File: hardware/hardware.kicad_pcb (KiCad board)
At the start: 4 copper layers, 100 parts, among them IC1 TAS5760LDAPR, J2 Conn_01x04, J3 Conn_01x04, J4 USB-C, SW1 SW_Push, SW2 SW_Push, SW3 SW_Push, SW5 SW_Push, U1 TPS563200, U2 ESP32-S3, U3 USBLC6-2SC6, Y1 40MHz, Y2 ABS07-166-32.768KHZ-T

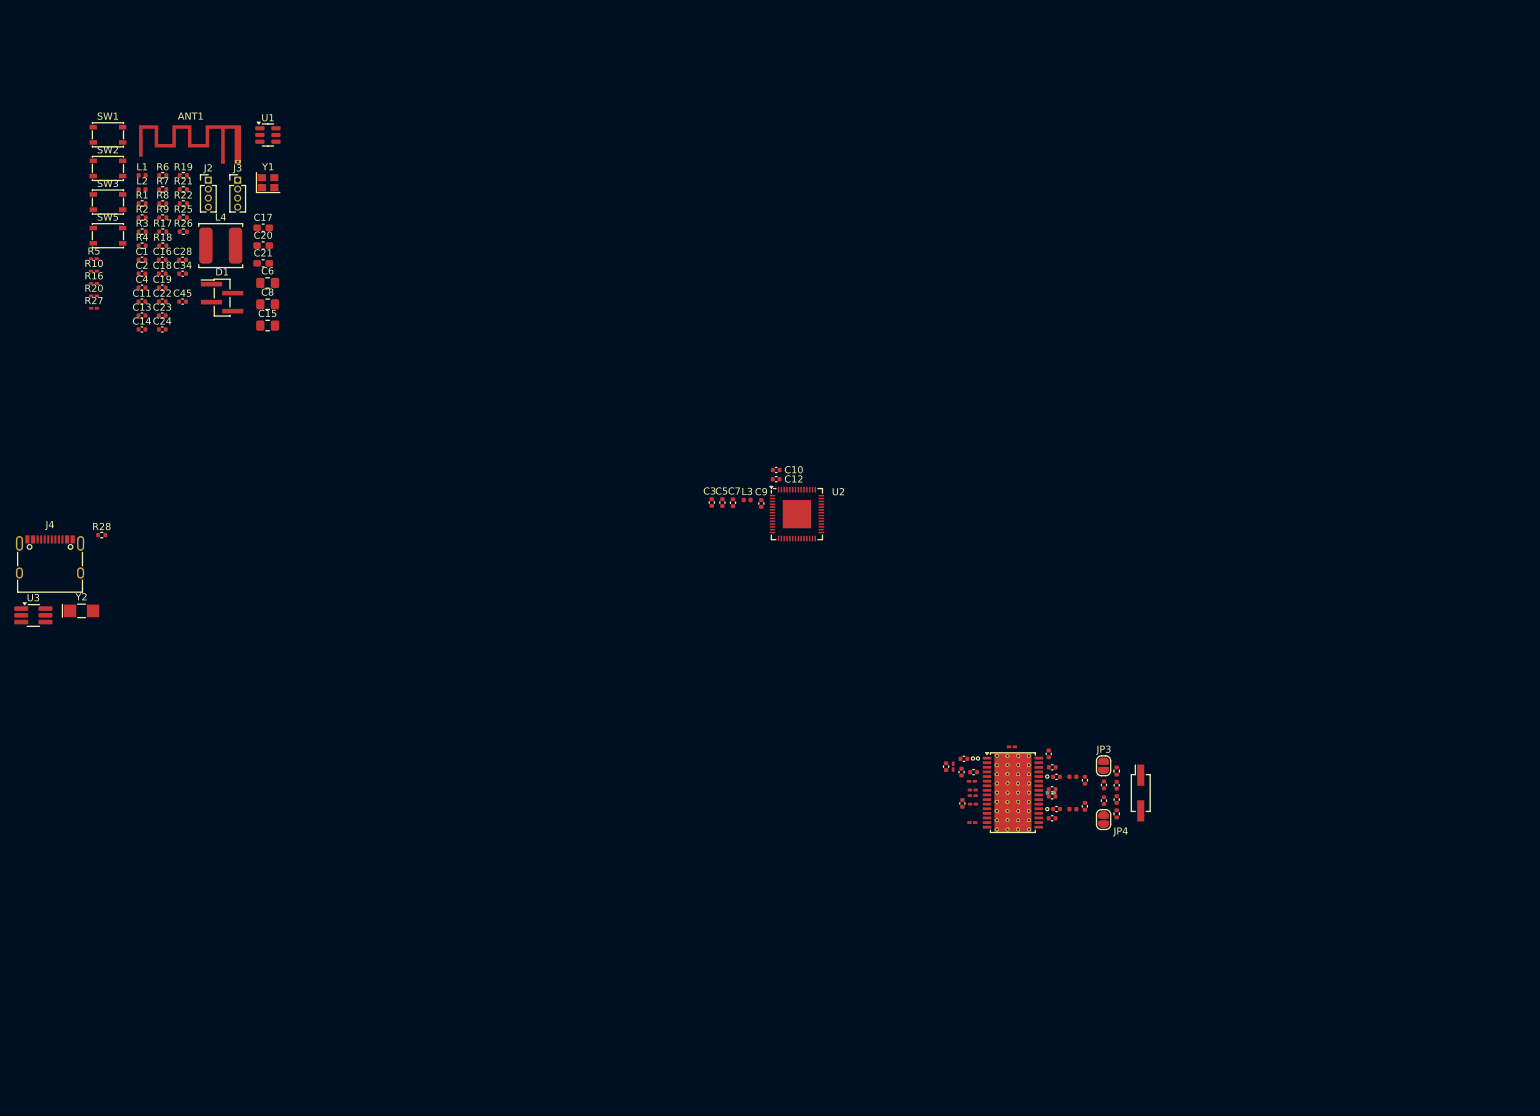
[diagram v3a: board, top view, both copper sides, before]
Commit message: roteamentos do amplificador, perifericos agrupados
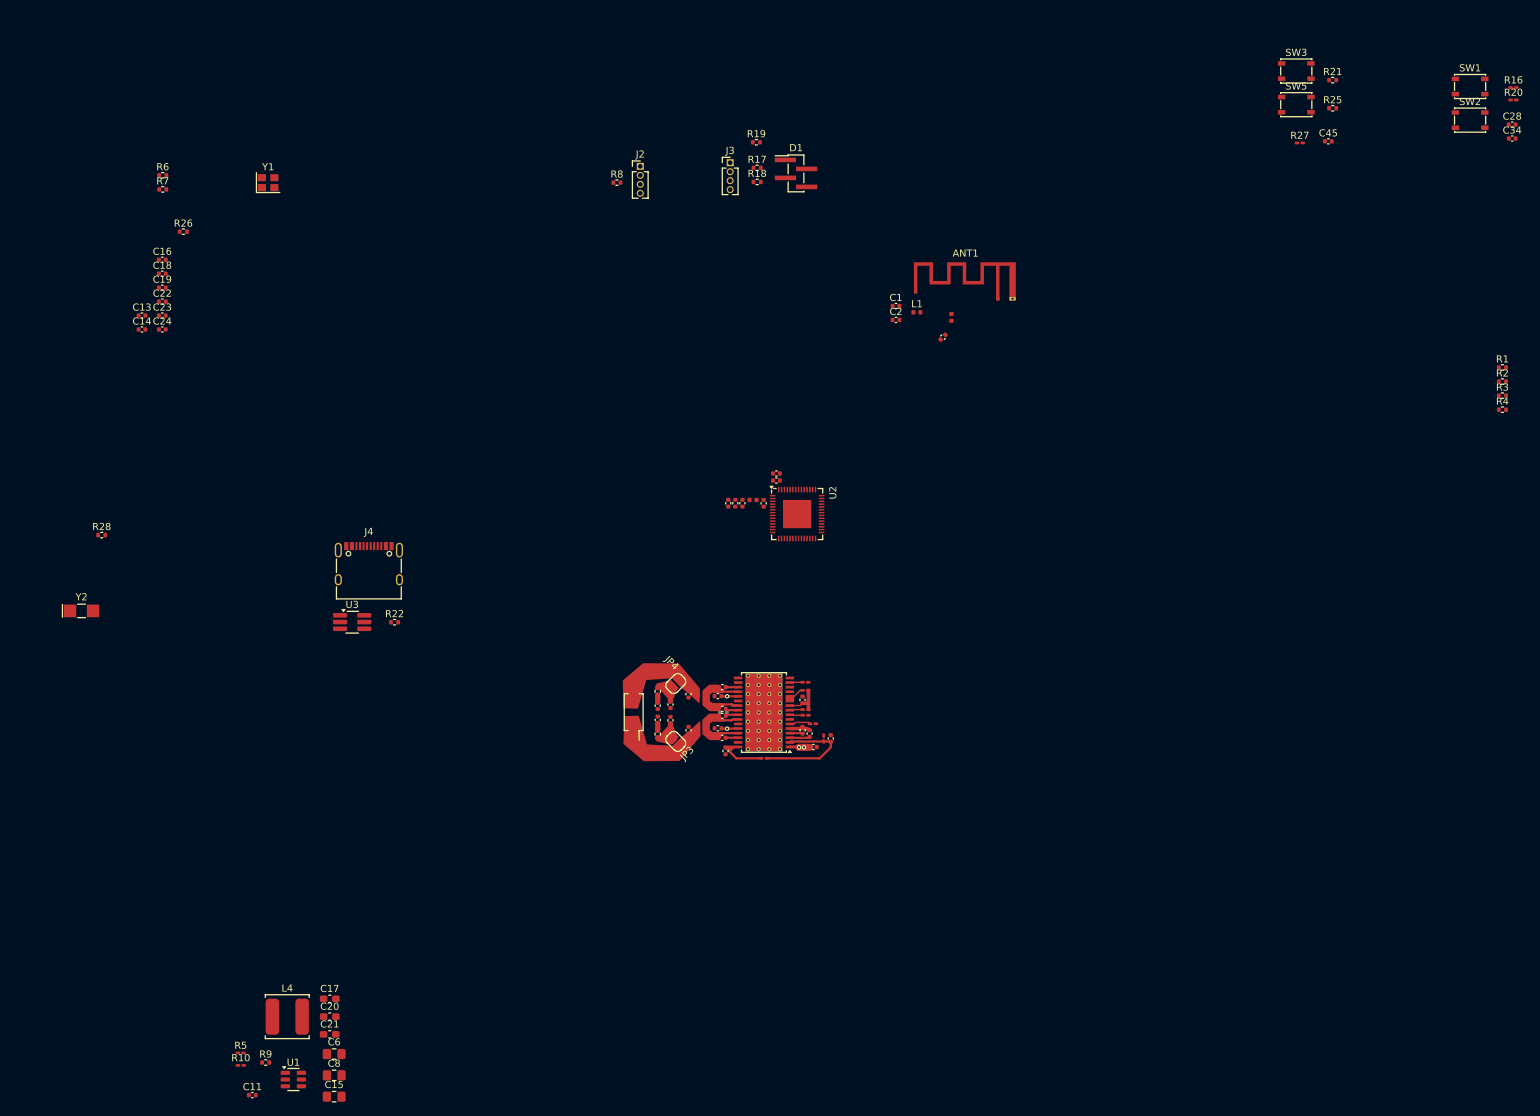
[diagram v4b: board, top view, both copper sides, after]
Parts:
- moved R16 202.4 mm to (240.2, 28.4)
- moved R20 202.4 mm to (240.2, 30.1)
- moved R1 193.5 mm to (238.7, 67.9)
- moved R2 193.5 mm to (238.7, 69.9)
- moved R3 193.5 mm to (238.7, 71.9)
- moved R4 193.5 mm to (238.7, 73.9)
- moved SW1 192.5 mm to (234.1, 28.2)
- moved SW2 192.5 mm to (234.1, 33.0)
- moved C28 188.8 mm to (240.1, 33.6)
- moved C34 188.8 mm to (240.1, 35.6)
- moved R27 171.9 mm to (210.1, 36.2)
- moved SW3 168.9 mm to (209.6, 26.0)
- moved SW5 168.9 mm to (209.6, 30.8)
- moved C45 163.4 mm to (214.1, 36.0)
- moved R21 163.1 mm to (214.7, 27.3)
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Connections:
- U2 pad 10: AUDIO_MUTE -> JTAG
- U2 pad 11: AUDIO_CLK -> AUDIO_EN
- U2 pad 12: I2C_CLK -> AUDIO_FAULT
- U2 pad 13: SDIN -> BOOT
- U2 pad 14: LRCK -> EN
- U2 pad 4: EN -> LRCK
- U2 pad 5: BOOT -> SDIN
- U2 pad 6: AUDIO_FAULT -> I2C_CLK
- U2 pad 7: AUDIO_EN -> AUDIO_CLK
- U2 pad 8: JTAG -> AUDIO_MUTE
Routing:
- net Net-(IC1-SFT_CLIP): track 0.00 -> 16.1 mm
- net Net-(IC1-SPK_OUTB+): track 0.00 -> 15.1 mm
- net Net-(IC1-SPK_OUTA+): track 0.00 -> 13.6 mm
- net Net-(JP4-A): track 0.00 -> 11.8 mm
- net Net-(JP3-B): track 0.00 -> 11.7 mm
- net 8V: track 0.00 -> 9.12 mm, vias 0 -> 4
- net Net-(IC1-GVDD_REG): track 0.00 -> 7.64 mm
- net 3V3: track 0.00 -> 5.50 mm
- net Net-(JP3-A): track 0.00 -> 5.07 mm
- net Net-(JP4-B): track 0.00 -> 4.34 mm
- net Net-(IC1-ANA_REF): track 0.00 -> 3.17 mm
- net AUDIO_FAULT: track 0.00 -> 3.03 mm
- net Net-(IC1-ANA_REG): track 0.00 -> 2.97 mm
- net Net-(IC1-SPK_GAIN0): track 0.00 -> 2.43 mm
- net Net-(IC1-BSTRPB-): track 0.00 -> 1.98 mm
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
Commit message: usb
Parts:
- added ?: , , F.Cu at (139.4, 118.6)
- U3: footprint Package_TO_SOT_SMD:TSOT-23-6_HandSoldering -> SamacSys_Parts:SOT95P280X145-6N
- moved R13 76.4 mm to (213.1, 136.8)
- moved C25 76.4 mm to (212.6, 138.1)
- moved C35 76.4 mm to (196.5, 142.4)
- moved C36 76.4 mm to (196.5, 137.3)
- moved C39 76.4 mm to (200.7, 137.6)
- moved C40 76.4 mm to (194.0, 141.0)
- moved C43 76.4 mm to (192.2, 140.9)
- moved L6 76.4 mm to (198.4, 137.6)
- moved R12 76.4 mm to (213.1, 139.5)
- moved R14 76.4 mm to (213.1, 140.3)
- moved R23 76.4 mm to (192.2, 142.9)
- moved R24 76.4 mm to (192.2, 136.9)
- moved C27 76.4 mm to (212.7, 142.4)
- moved C29 76.4 mm to (201.3, 139.4)
- moved C30 76.4 mm to (201.8, 145.3)
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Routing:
- net +5V: track 0.00 -> 14.7 mm, vias 0 -> 3
- net /CC1: track 0.00 -> 9.41 mm
- net /D-: track 0.00 -> 7.21 mm
- net /D+: track 0.00 -> 5.82 mm
- net GND: track 0.00 -> 3.78 mm, vias 0 -> 1
- net USB_DP: track 0.00 -> 1.20 mm
- net USB_DN: track 0.00 -> 1.05 mm

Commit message: desacoplamento
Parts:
- Y1: value 40MHz -> ECS-400-10-36B2-CKM-TR
- moved R1 119.7 mm to (123.1, 98.9), turned to -90 degrees
- moved R3 117.6 mm to (124.2, 98.9), turned to -90 degrees
- moved R2 117.0 mm to (125.3, 98.9), turned to -90 degrees
- moved R4 115.0 mm to (126.4, 98.9), turned to -90 degrees
- moved R28 108.9 mm to (149.6, 97.0), turned to -90 degrees
- moved R26 107.6 mm to (148.5, 97.0), turned to -90 degrees
- moved R7 107.5 mm to (141.8, 97.8), turned to 90 degrees
- moved Y2 101.9 mm to (139.8, 98.3), turned to -90 degrees
- moved C18 101.8 mm to (139.6, 101.8), turned to 180 degrees
- moved C24 100.3 mm to (145.7, 90.7), turned to -90 degrees
- moved C23 99.9 mm to (144.6, 90.7), turned to -90 degrees
- moved C16 98.1 mm to (137.9, 94.9), turned to 90 degrees
- moved C19 97.4 mm to (137.9, 97.2), turned to 90 degrees
- moved C13 96.8 mm to (141.0, 81.9), turned to -90 degrees
- moved R6 95.8 mm to (136.7, 80.3), turned to -90 degrees
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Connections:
- Y1 pad 1: Net-(U2-XTAL_N) -> Net-(C14-Pad1)
- Y1 pad 3: GPIO_45_46 -> Net-(U2-XTAL_N)
- Y1 pad 4: Net-(C14-Pad1) -> GPIO_45_46
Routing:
- net 3V3: track 5.50 -> 23.7 mm, vias 0 -> 4
- net Net-(ANT1-Pad1): track 0.00 -> 13.6 mm
- net Net-(U2-XTAL_32K_P): track 0.00 -> 7.29 mm
- net Net-(U2-XTAL_32K_N): track 0.00 -> 6.29 mm
- net Net-(C9-Pad2): track 0.00 -> 5.92 mm
- net Net-(C18-Pad1): track 0.00 -> 5.67 mm
- net Net-(U2-XTAL_N): track 0.00 -> 5.31 mm
- net Display_SDA: track 0.00 -> 4.82 mm
- net Net-(U2-GPIO19/USB_D-): track 0.00 -> 4.78 mm
- net Net-(U2-XTAL_P): track 0.00 -> 4.57 mm
- net BT_L: track 0.00 -> 4.45 mm
- net VBAT: track 0.00 -> 4.39 mm, vias 0 -> 1
- net Display_SCL: track 0.00 -> 4.31 mm
- net Net-(U2-GPIO20/USB_D+): track 0.00 -> 4.31 mm
- net Net-(U2-LNA_IN): track 0.00 -> 4.18 mm, vias 0 -> 1
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
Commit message: cartao de memoria e usb
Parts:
- added J1: 798-DM3D-SF, Connector_Card:microSD_HC_Hirose_DM3D-SF, B.Cu at (131.1, 105.3)
- ?, J4, R22, U3: moved to B.Cu
- J2, J3: footprint Connector_PinHeader_1.27mm:PinHeader_1x04_P1.27mm_Vertical -> Connector_PinHeader_1.27mm:PinHeader_1x04_P1.27mm_Vertical_SMD_Pin1Left
- moved C25 106.1 mm to (111.7, 105.5)
- moved C33 106.1 mm to (100.4, 107.8)
- moved C35 106.1 mm to (95.6, 109.8)
- moved C36 106.1 mm to (95.6, 104.7)
- moved C40 106.1 mm to (93.1, 108.4)
- moved C41 106.1 mm to (93.1, 106.2)
- moved L6 106.1 mm to (97.4, 104.9)
- moved R12 106.1 mm to (112.1, 106.9)
- moved R13 106.1 mm to (112.1, 104.1)
- moved R14 106.1 mm to (112.1, 107.7)
- moved C26 106.1 mm to (112.7, 110.2)
- moved C27 106.1 mm to (111.7, 109.8)
- moved C29 106.1 mm to (100.4, 106.8)
- moved C30 106.1 mm to (100.8, 112.7)
- moved C31 106.1 mm to (100.4, 110.9)
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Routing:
- net 3V3: track 23.7 -> 41.5 mm, vias 4 -> 6
- net uCHIP_DI: track 0.00 -> 10.7 mm, vias 0 -> 1
- net uCHIP_SCK: track 0.00 -> 10.3 mm, vias 0 -> 1
- net uCHIP_DO: track 0.00 -> 9.98 mm, vias 0 -> 1
- net Display_SCL: track 4.31 -> 13.6 mm
- net Net-(U2-GPIO10): track 2.31 -> 9.92 mm
- net USB_DN: track 1.05 -> 7.99 mm, vias 0 -> 1
- net Net-(U2-GPIO11): track 2.67 -> 9.37 mm
- net Net-(U2-GPIO12): track 3.01 -> 9.34 mm
- net USB_DP: track 1.20 -> 7.17 mm, vias 0 -> 1
- net Net-(U2-GPIO13): track 4.02 -> 9.21 mm
- net Display_SDA: track 4.82 -> 8.76 mm
- net BT_R: track 2.54 -> 4.37 mm
- net Net-(U2-GPIO20/USB_D+): track 4.31 -> 3.11 mm
- net Net-(U2-GPIO19/USB_D-): track 4.78 -> 3.65 mm
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
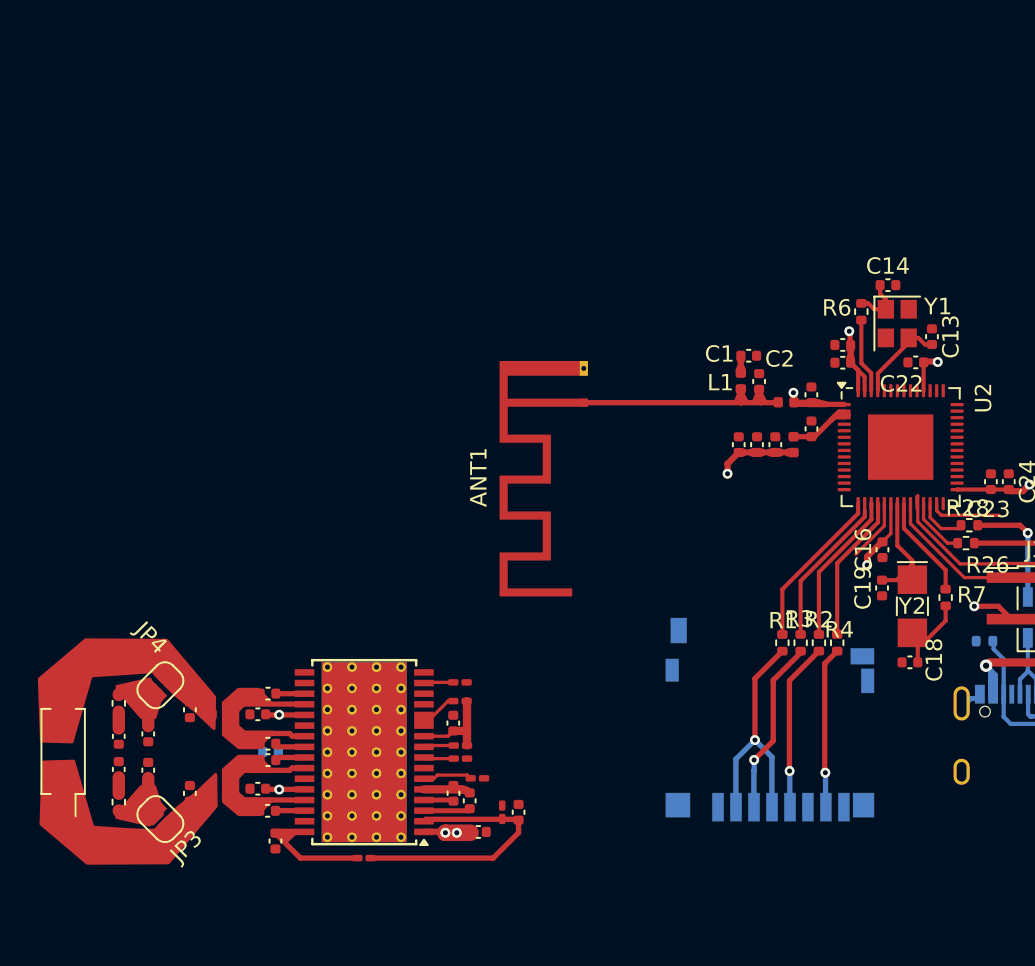
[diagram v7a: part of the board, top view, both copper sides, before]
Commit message: coloquei a antena para cima para liberar espaço para o amplificador de som; adicionei algumas vias de terra
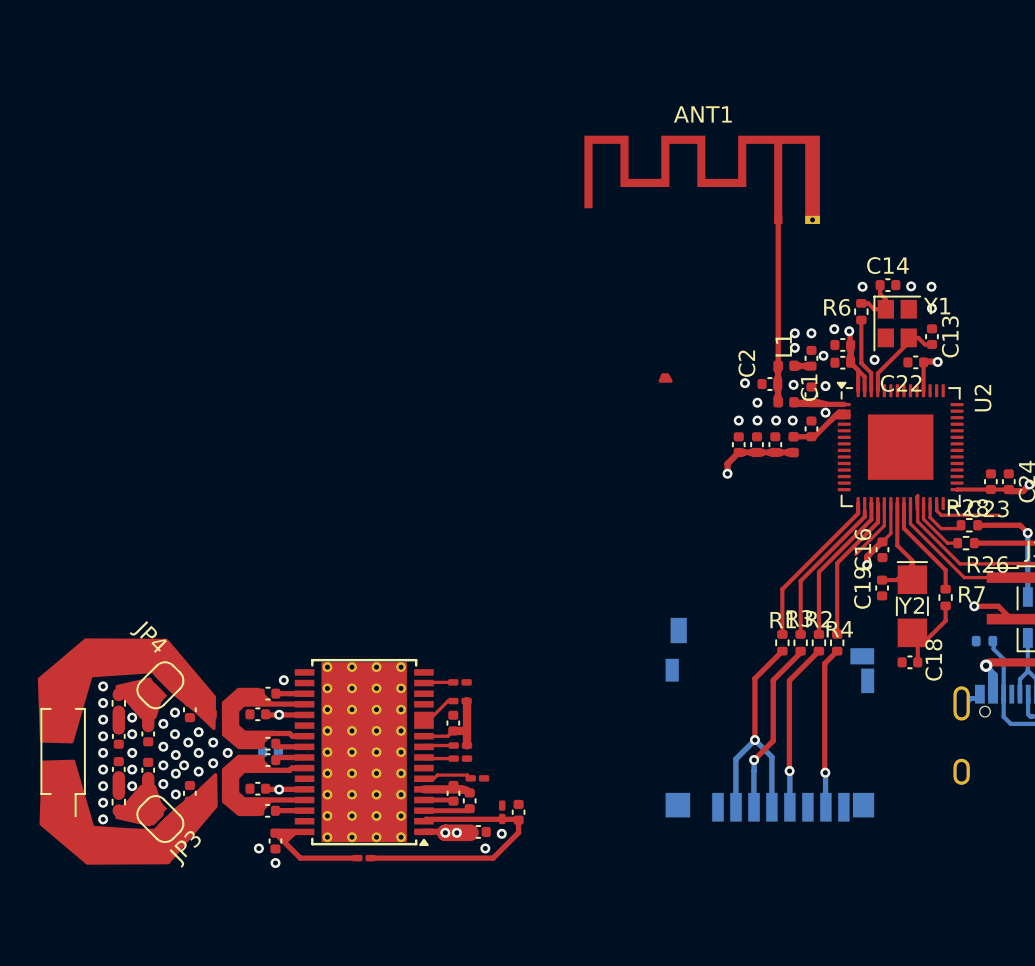
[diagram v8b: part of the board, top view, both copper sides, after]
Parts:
- moved ANT1 16.3 mm to (131.6, 74.7), turned to 0 degrees
- moved C1 3.84 mm to (133.6, 83.2), turned to -90 degrees
- moved L1 2.92 mm to (132.1, 83.6), turned to 0 degrees
- moved C2 0.68 mm to (131.1, 84.8), turned to 0 degrees
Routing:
- net Net-(ANT1-Pad1): track 13.6 -> 11.2 mm
- net Net-(U2-LNA_IN): vias 1 -> 0
- net GND: vias 1 -> 56
